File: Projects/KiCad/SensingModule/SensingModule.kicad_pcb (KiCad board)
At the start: 2 copper layers, 110 x 95 mm, 42 parts, among them J1 Conn_01x05_Socket, J2 Conn_01x02_Pin, J3 Conn_01x05_Pin, J4 Micro_SD_Card_Det_Hirose_DM3AT, SW1 SW_Push, SW2 SW_Push, U2 NUCLEO-F303K8, U4 MCP2562-E-P, U5 TLP222A, U6 MB85RS2MT, U7 MB85RS2MT

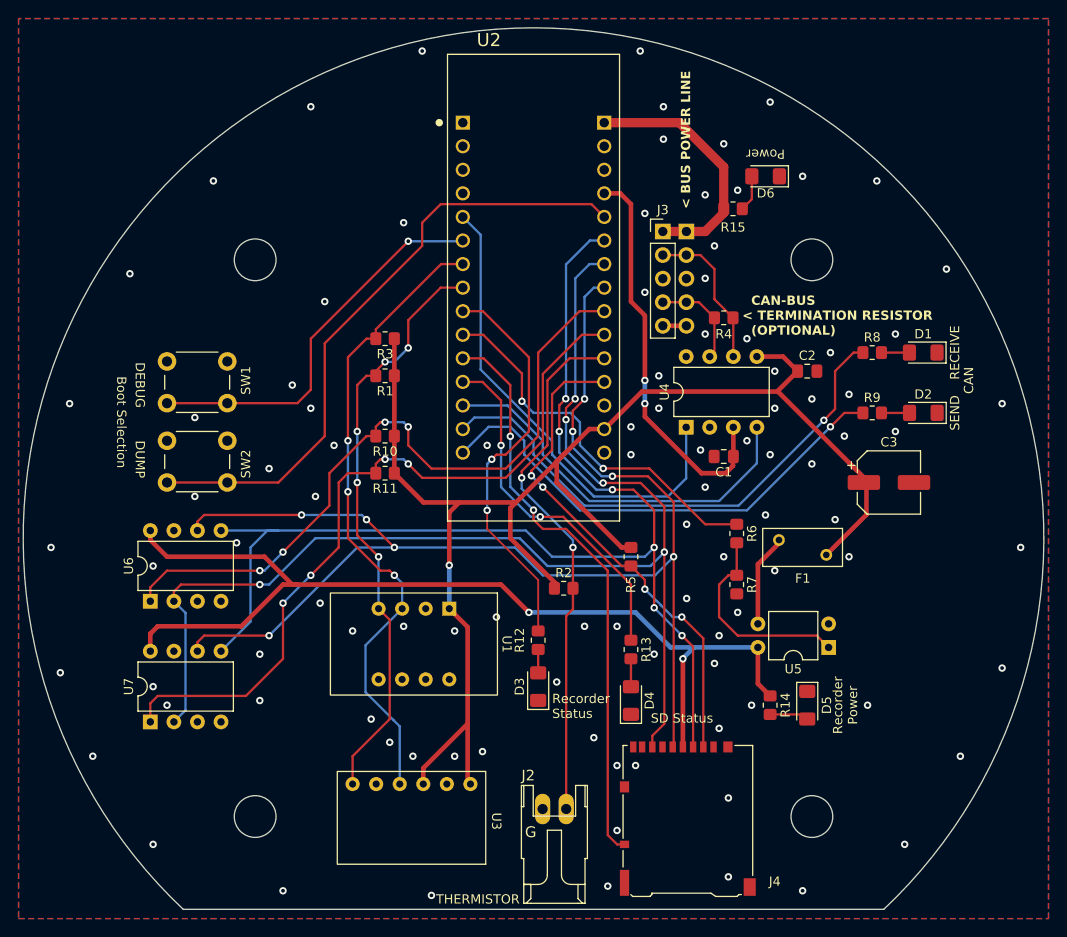
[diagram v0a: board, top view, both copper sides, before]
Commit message: 抵抗とLEDを1608に変更
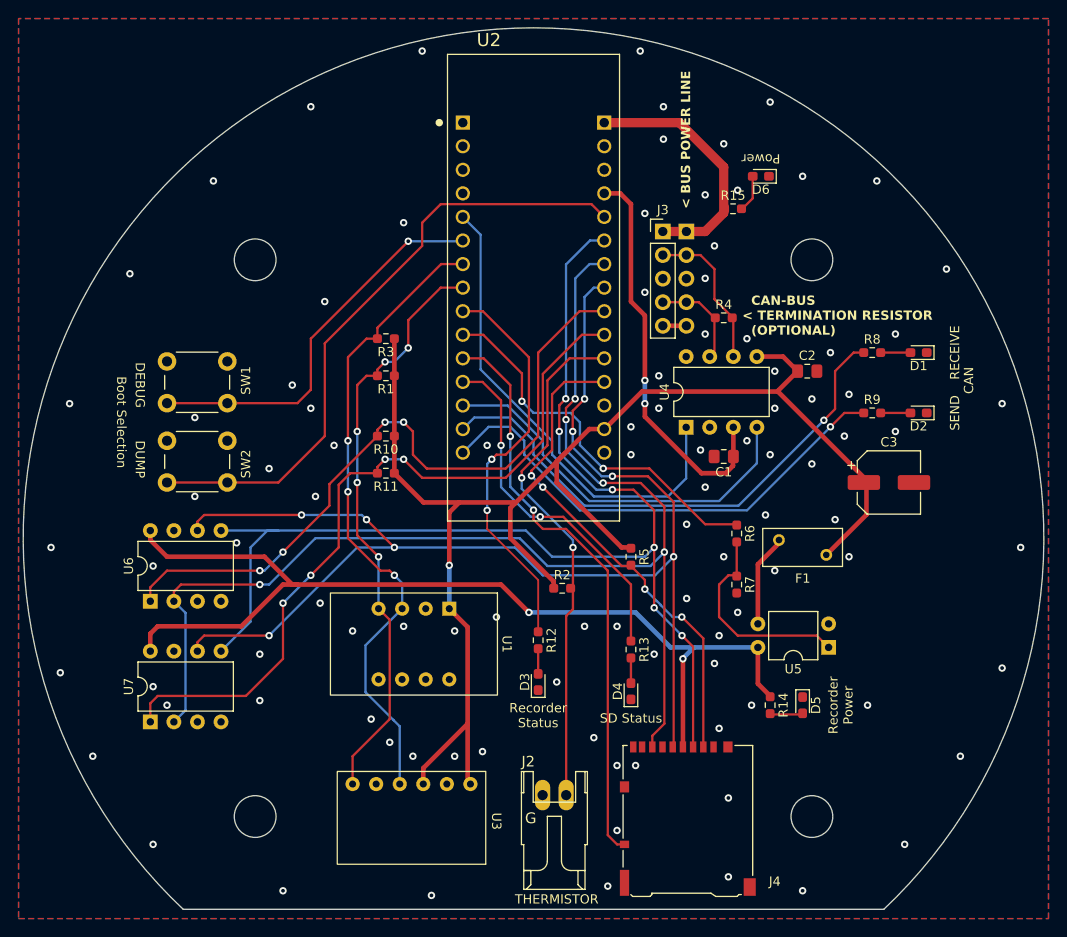
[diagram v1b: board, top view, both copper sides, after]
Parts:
- D1, D2, D3, D4, D5, D6: footprint LED_SMD:LED_1206_3216Metric_Pad1.42x1.75mm_HandSolder -> LED_SMD:LED_0603_1608Metric_Pad1.05x0.95mm_HandSolder
- R1, R10, R11, R12, R13, R14, R15, R2, R3, R4, R5, R6, R7, R8, R9: footprint Resistor_SMD:R_0805_2012Metric_Pad1.20x1.40mm_HandSolder -> Resistor_SMD:R_0603_1608Metric_Pad0.98x0.95mm_HandSolder
- moved J2 1.50 mm to (150.8, 136.5)
- moved D4 1.00 mm to (159.0, 121.5)
- moved D2 0.51 mm to (190.0, 91.5)
- moved D6 0.51 mm to (173.0, 66.0)
- moved D1 0.50 mm to (190.0, 85.0)
- moved D3 0.50 mm to (149.0, 120.5)
- moved D5 0.50 mm to (177.5, 123.0)
- moved R2 0.16 mm to (151.6, 110.4)
- moved R1 0.09 mm to (132.6, 87.5)
- moved R10 0.09 mm to (132.6, 94.0)
- moved R11 0.09 mm to (132.6, 98.0)
- moved R3 0.09 mm to (132.6, 83.5)
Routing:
- net THERMISTOR: track 57.0 -> 55.5 mm
- net SPI_CS_FRAM1: track 76.0 -> 75.4 mm

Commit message: 抵抗値を調整
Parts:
- R12, R13: value 100Ω -> 300Ω
- R14: value 1kΩ -> 300Ω
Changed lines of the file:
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@@
         (effects (font (size 1 1) (thickness 0.15)))
     )
-    (fp_text value "100Ω" (at 0 1.43 -90) (layer "F.Fab")
+    (fp_text value "300Ω" (at 0 1.43 -90) (layer "F.Fab")
         (effects (font (size 1 1) (thickness 0.15)))
     )
@@
         (effects (font (size 1 1) (thickness 0.15)))
     )
-    (fp_text value "100Ω" (at 0 1.43 -90) (layer "F.Fab")
+    (fp_text value "300Ω" (at 0 1.43 -90) (layer "F.Fab")
         (effects (font (size 1 1) (thickness 0.15)))
     )
@@
         (effects (font (size 1 1) (thickness 0.15)))
     )
-    (fp_text value "1kΩ" (at 0 1.43 -90) (layer "F.Fab")
-        (effects (font (size 1 1) (thickness 0.15)))
-    )
+    (fp_text value "300Ω" (at 0 1.43 -90) (layer "F.Fab")
+        (effects (font (size 1 1) (thickness 0.15)))
+    )

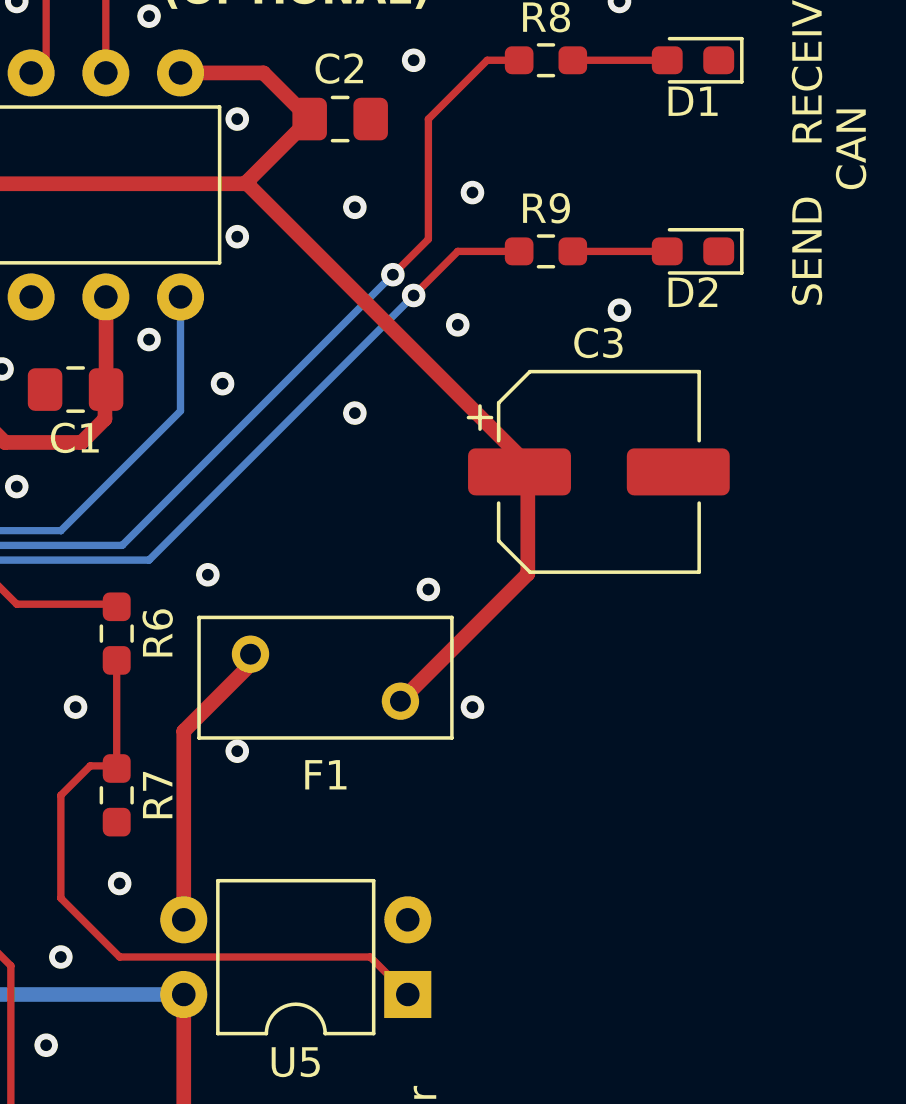
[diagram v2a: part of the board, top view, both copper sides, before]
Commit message: リセッタブルフューズをSMDに変更
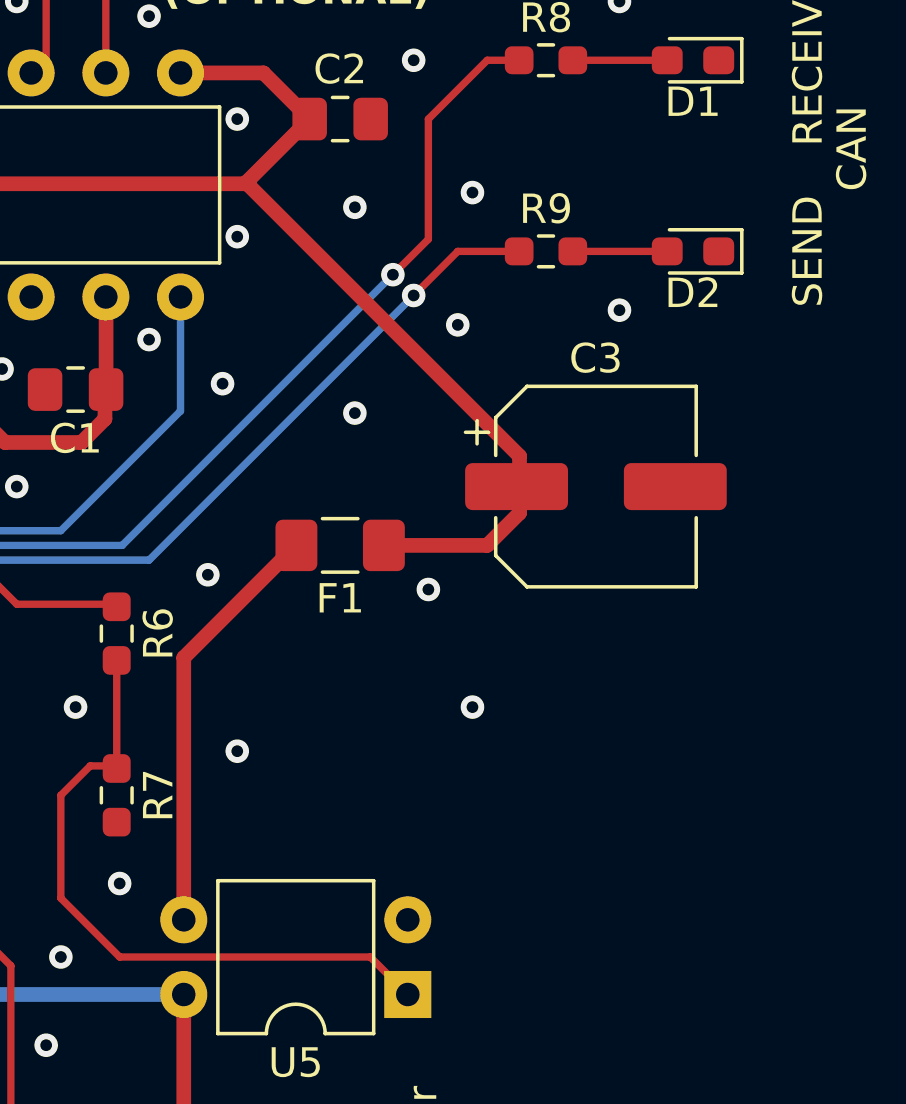
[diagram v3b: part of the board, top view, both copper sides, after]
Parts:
- F1: footprint Fuse:Fuse_BelFuse_0ZRE0005FF_L8.3mm_W3.8mm -> Fuse:Fuse_1206_3216Metric_Pad1.42x1.75mm_HandSolder
- moved F1 5.68 mm to (178.0, 101.5)
- moved C3 0.51 mm to (186.7, 99.5)
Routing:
- net Net-(F1-Pad2): track 9.77 -> 14.3 mm
- net +3.3V: track 159.5 -> 156.4 mm

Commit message: 一通り部品を選定
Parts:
- D1, D2: value LED -> ORANGE
- D3, D4: value LED -> GREEN
- D5, D6: value LED -> RED
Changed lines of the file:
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@@
         (effects (font (size 1 1) (thickness 0.15)))
     )
-    (fp_text value "LED" (at 0 1.43 90) (layer "F.Fab")
+    (fp_text value "GREEN" (at 0 1.43 90) (layer "F.Fab")
         (effects (font (size 1 1) (thickness 0.15)))
     )
@@
         (effects (font (size 1 1) (thickness 0.15)))
     )
-    (fp_text value "LED" (at 0 1.43 90) (layer "F.Fab")
+    (fp_text value "GREEN" (at 0 1.43 90) (layer "F.Fab")
         (effects (font (size 1 1) (thickness 0.15)))
     )
@@
         (effects (font (size 1 1) (thickness 0.15)))
     )
-    (fp_text value "LED" (at 0 1.43 180) (layer "F.Fab")
+    (fp_text value "ORANGE" (at 0 1.43 180) (layer "F.Fab")
         (effects (font (size 1 1) (thickness 0.15)))
     )
@@
         (effects (font (size 1 1) (thickness 0.15)))
     )
-    (fp_text value "LED" (at 0 1.43 180) (layer "F.Fab")
+    (fp_text value "ORANGE" (at 0 1.43 180) (layer "F.Fab")
         (effects (font (size 1 1) (thickness 0.15)))
     )
@@
         (effects (font (size 1 1) (thickness 0.15)))
     )
-    (fp_text value "LED" (at 0 1.43 180) (layer "F.Fab")
+    (fp_text value "RED" (at 0 1.43 180) (layer "F.Fab")
         (effects (font (size 1 1) (thickness 0.15)))
     )
@@
         (effects (font (size 1 1) (thickness 0.15)))
     )
-    (fp_text value "LED" (at 0 1.43 -90) (layer "F.Fab")
-        (effects (font (size 1 1) (thickness 0.15)))
-    )
+    (fp_text value "RED" (at 0 1.43 -90) (layer "F.Fab")
+        (effects (font (size 1 1) (thickness 0.15)))
+    )

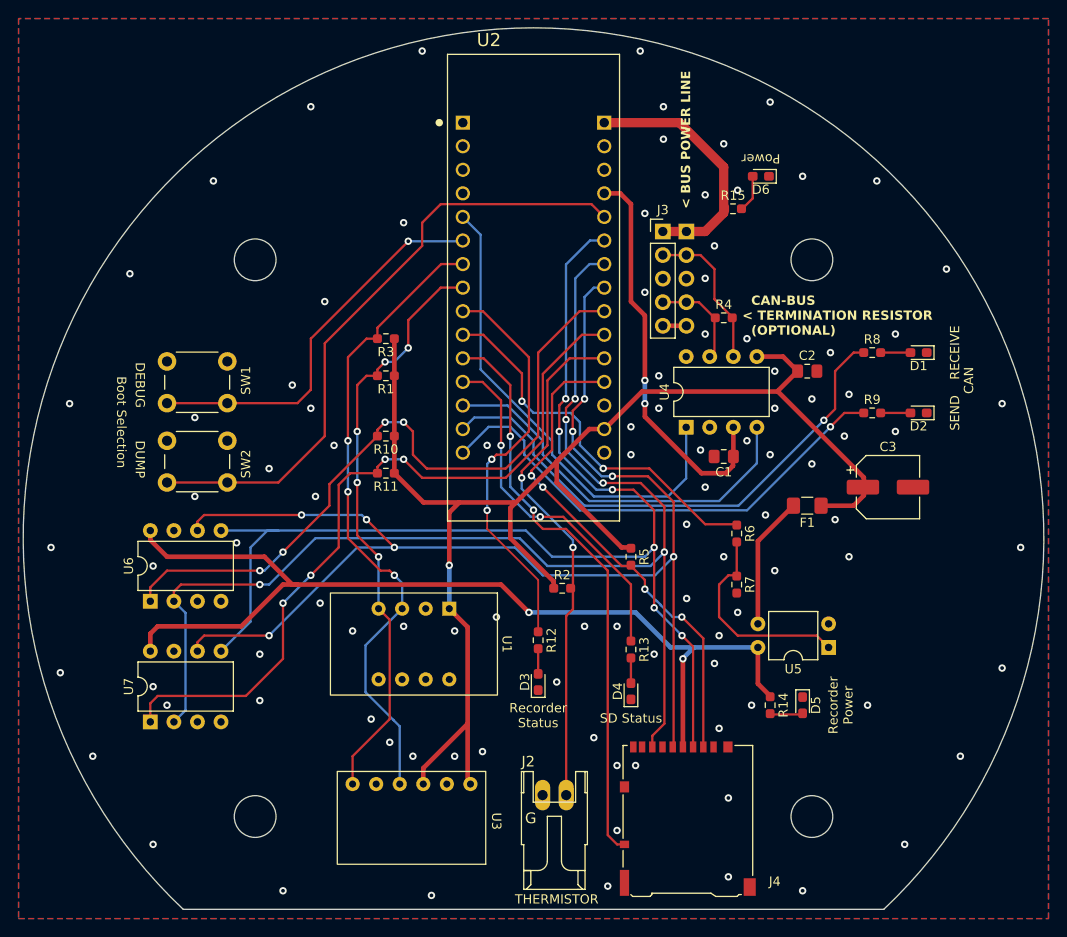
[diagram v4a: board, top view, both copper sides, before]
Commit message: 計測モジュールとフライトモジュールのコネクタを再配置
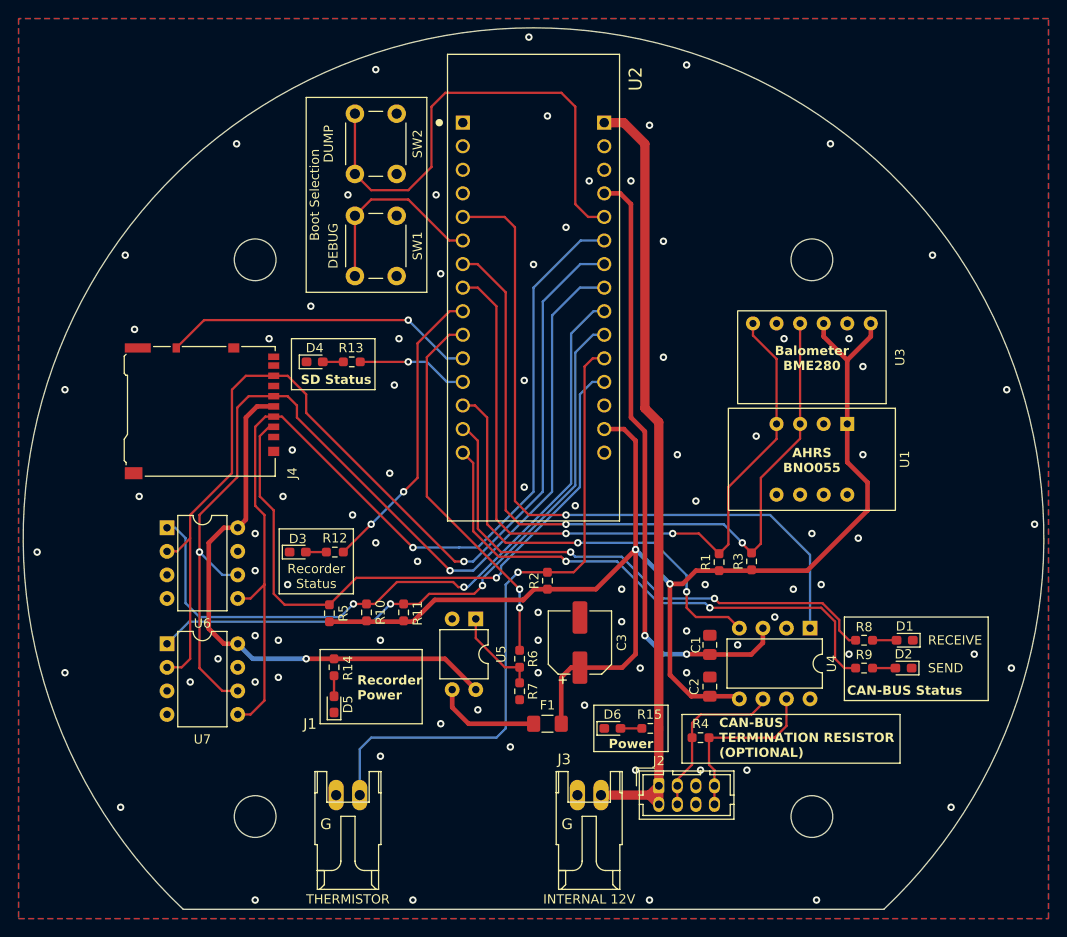
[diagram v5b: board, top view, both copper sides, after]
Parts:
- removed the J1 at (165.0, 72.0)
- added J2: Conn_01x08, Connector_Hirose:Hirose_DF11-8DP-2DSA_2x04_P2.00mm_Vertical, F.Cu at (162.0, 131.7)
- J3: value Conn_01x05_Pin -> Conn_01x02; footprint Connector_PinHeader_2.54mm:PinHeader_1x05_P2.54mm_Vertical -> Hirose_Connector:Hirose_DF1B
- moved J4 68.3 mm to (112.8, 91.3), turned to -90 degrees
- moved U3 65.8 mm to (186.5, 90.5)
- moved D6 61.6 mm to (157.0, 125.5), turned to 0 degrees
- moved J3 61.4 mm to (153.2, 132.7)
- moved R15 56.7 mm to (161.1, 125.5), turned to 180 degrees
- moved D5 50.5 mm to (127.0, 122.9), turned to 90 degrees
- moved D4 49.2 mm to (124.9, 86.0), turned to 0 degrees
- moved U1 47.3 mm to (187.4, 96.5)
- moved R14 47.2 mm to (127.0, 118.9)
- moved R3 46.1 mm to (172.0, 107.5), turned to 90 degrees
- moved R4 45.3 mm to (166.5, 126.5), turned to 180 degrees
- moved R13 43.2 mm to (128.9, 86.0), turned to 180 degrees
- moved SW2 43.1 mm to (133.8, 59.2), turned to -90 degrees
- moved R1 41.1 mm to (168.5, 107.6), turned to 90 degrees
- moved U5 38.1 mm to (142.3, 113.7), turned to -90 degrees
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- renumbered J2 to J1
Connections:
- J3 pad 1: +12V -> GND
- J3 pad 2: CAN_L -> +12V
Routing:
- net +12V: track 27.2 -> 85.2 mm
- net MEMORY_POWER: track 108.2 -> 60.3 mm, vias 2 -> 1
- net SD_CHECK: track 62.8 -> 33.8 mm, vias 2 -> 1
- net SPI_SCLK: track 141.4 -> 112.4 mm, vias 8 -> 2
- net SD_STATUS: track 38.6 -> 11.9 mm, vias 2 -> 1
- net CAN_TX: track 52.2 -> 77.7 mm, vias 0 -> 1
- net SPI_MOSI: track 130.3 -> 107.4 mm, vias 6 -> 1
- net SPI_MISO: track 134.4 -> 112.3 mm, vias 5 -> 1
- net DEBUG_MODE: track 42.4 -> 20.7 mm, vias 1 -> 0
- net +5V: track 45.9 -> 66.1 mm
- net SPI_CS_SD: track 54.0 -> 71.9 mm, vias 4 -> 1
- net I2C_SCL: track 63.8 -> 81.4 mm, vias 5 -> 2
- net I2C_SDA: track 69.4 -> 84.7 mm, vias 3 -> 2
- net THERMISTOR: track 55.5 -> 70.1 mm, vias 2 -> 1
- net DUMP_MODE: track 67.4 -> 53.9 mm
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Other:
- board text added: "AHRS BNO055"
- board text added: "Balometer BME280"
- board text added: "CAN-BUS Status"
- board text added: "CAN-BUS TERMINATION RESISTOR (OPTIONAL)"
- board text added: "INTERNAL 12V"
- board text removed: "< BUS POWER LINE"
- board text removed: "CAN"
- board text removed: "CAN-BUS < TERMINATION RESISTOR (OPTIONAL)"

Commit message: コネクタを再配置, 基板上で12V->5Vをするように変更
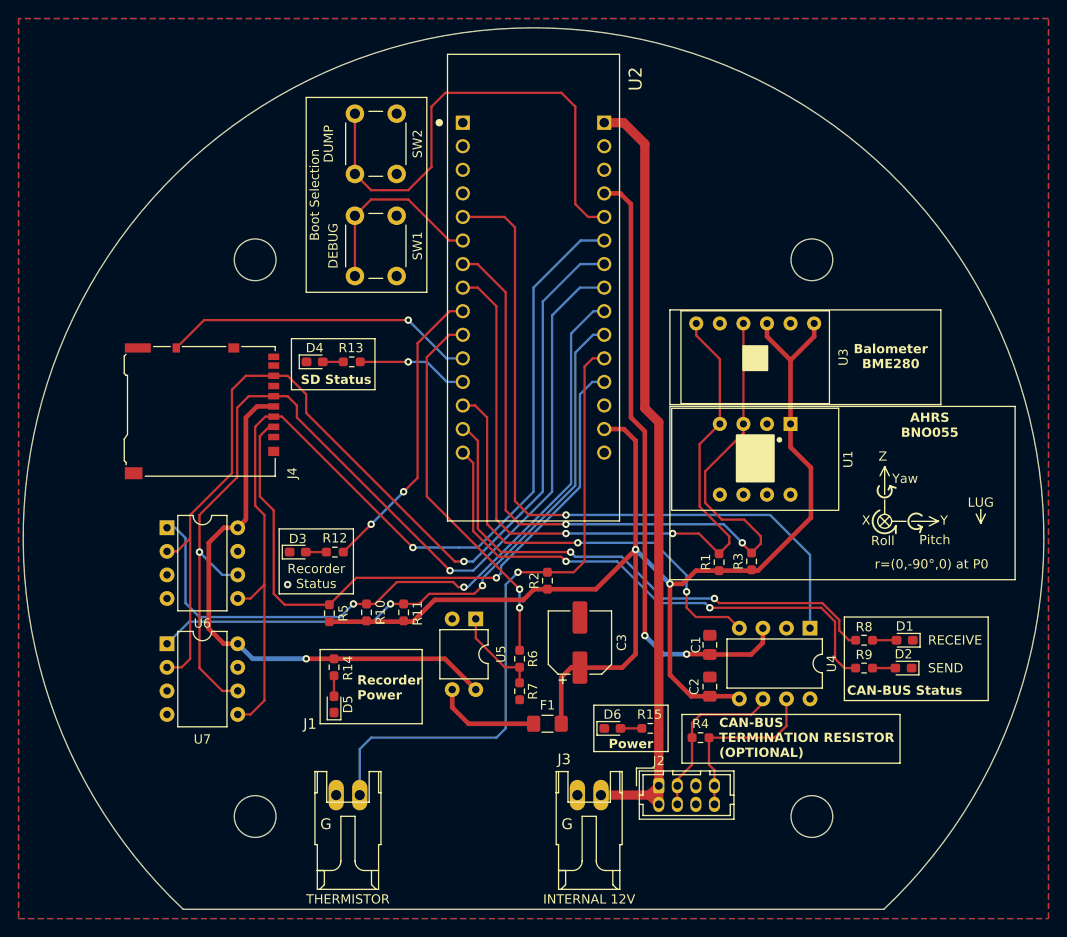
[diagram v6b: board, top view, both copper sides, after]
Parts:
- moved U1 6.11 mm to (181.3, 96.5)
- moved U3 6.11 mm to (180.4, 90.5)
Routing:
- net +3.3V: track 152.5 -> 146.8 mm
- net I2C_SDA: track 84.7 -> 88.6 mm
- net GND: vias 87 -> 1
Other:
- board text added: "LUG"
- board text added: "Pitch"
- board text added: "Roll"
- board text added: "X"
- board text added: "Y"
- board text added: "Yaw"
- board text added: "Z"
- board text added: "r=(0,-90°,0) at P0"

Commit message: 基板設計の都市伝説をいろいろ適応
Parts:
- removed the REF** at (178.5, 75.0)
- removed the REF** at (118.5, 135.0)
- removed the REF** at (178.5, 135.0)
- removed the REF** at (118.5, 75.0)
- added REF**: MountingHole_4.5mm_Pad_Via, MountingHole:MountingHole_4.5mm_Pad_Via, F.Cu at (118.5, 75.0)
- added REF**: MountingHole_4.5mm_Pad_Via, MountingHole:MountingHole_4.5mm_Pad_Via, F.Cu at (118.5, 135.0)
- added REF**: MountingHole_4.5mm_Pad_Via, MountingHole:MountingHole_4.5mm_Pad_Via, F.Cu at (178.5, 135.0)
- added REF**: MountingHole_4.5mm_Pad_Via, MountingHole:MountingHole_4.5mm_Pad_Via, F.Cu at (178.5, 75.0)
- moved R2 15.8 mm to (181.5, 121.4), turned to 90 degrees
- moved D2 1.61 mm to (190.0, 119.2)
- moved R3 1.61 mm to (185.7, 119.2)
- moved D1 1.59 mm to (190.1, 116.0)
- moved R1 1.59 mm to (185.7, 116.0)
- renumbered D6 to D3, D5 to D4, D3 to D5, D4 to D6, J3 to J1, J1 to J3, R8 to R1, R14 to R10, R12 to R11, R11 to R12, R10 to R13, R5 to R14, R13 to R15, R4 to R2, R9 to R3, R3 to R4, R1 to R5, R7 to R6, R15 to R7, R6 to R8, R2 to R9, U4 to U1, U3 to U2, U1 to U3, U5 to U4, U2 to U5, U7 to U6, U6 to U7
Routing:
- net CAN_L: track 18.4 -> 26.6 mm
- net CAN_H: track 19.2 -> 23.5 mm
- net +5V: track 66.1 -> 67.4 mm, vias 2 -> 5
- net CAN_TX: track 77.7 -> 76.6 mm, vias 1 -> 3
- net CAN_SEND_STATUS: track 58.6 -> 59.7 mm
- net SPI_CS_FRAM0: track 69.8 -> 69.0 mm
- net SPI_CS_SD: track 71.9 -> 71.2 mm
- net MEMORY_POWER: track 60.3 -> 60.9 mm, vias 1 -> 2
- net +12V: track 85.2 -> 84.7 mm
- net +3.3V: track 146.8 -> 146.7 mm, vias 2 -> 5
- net GND: vias 1 -> 169
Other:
- board text added: "CAN-BUS Termination Resistor"
- board text added: "Lug"
- board text removed: "CAN-BUS TERMINATION RESISTOR (OPTIONAL)"
- board text removed: "LUG"
